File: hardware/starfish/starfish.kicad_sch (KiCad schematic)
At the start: 3 parts

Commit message: First pass at schematic for starfish
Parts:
- added H104: GND, MountingHole:MountingHole_3mm_Pad, symbol Mechanical:MountingHole_Pad
- renumbered H1 to H101, H2 to H102, H3 to H103
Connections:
- net GND: now also H104.1
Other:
- sheet Left Motor renamed X Motor
- sheet Right Motor renamed Y2 Motor
- sheet Z Motor renamed Y1 Motor
- added sheet Buffer (buffer.kicad_sch)
- added sheet I2C Multiplexer (i2c_mux.kicad_sch)
- added sheet Pump A (pumps.kicad_sch)
- added sheet Pump B (pumps.kicad_sch)
- added sheet RS485 (rs485.kicad_sch)
- added sheet Vacuum sensor A (vacuum-sensors.kicad_sch)
- added sheet Vacuum sensor B (vacuum-sensors.kicad_sch)
- added sheet Valve A (solenoids.kicad_sch)
- added sheet Valve B (solenoids.kicad_sch)
- sheet Connections ports: added QWIIC1_SCK, QWIIC1_SDA, QWIIC2_SCK, QWIIC2_SDA; removed BLTOUCH_CONTROL, BLTOUCH_OUT, QWIIC_SCL, QWIIC_SDA
- sheet Microcontroller ports: added I2C_SCL, I2C_SDA, PUMP_A, PUMP_B, RS485_OUT_EN, RS485_RX, RS485_TX, RS485_~{IN_EN}, VALVE_A, VALVE_B; removed BLTOUCH_CONTROL, BLTOUCH_STATUS, QWIIC_SCL, QWIIC_SDA
- title: Candela Head -> Starfish
- moved on the sheet: H101, H102, H103

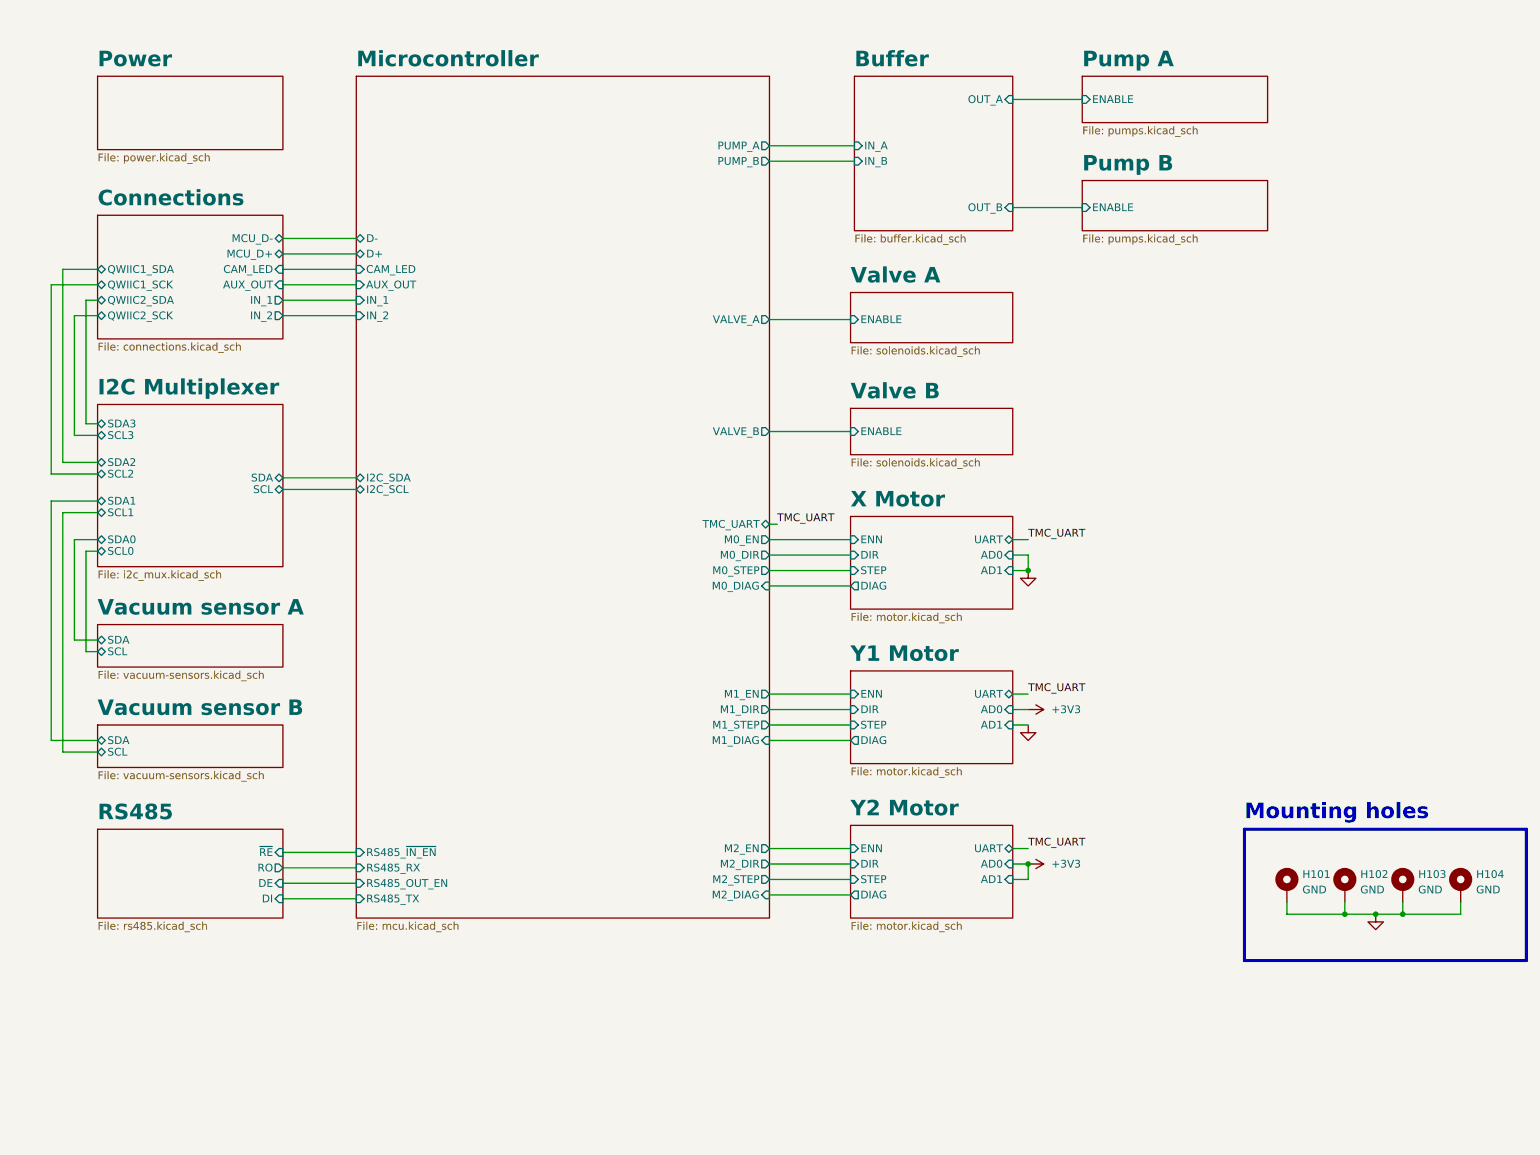
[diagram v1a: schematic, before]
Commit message: Mostly finished starfish schematic, ready for layout!
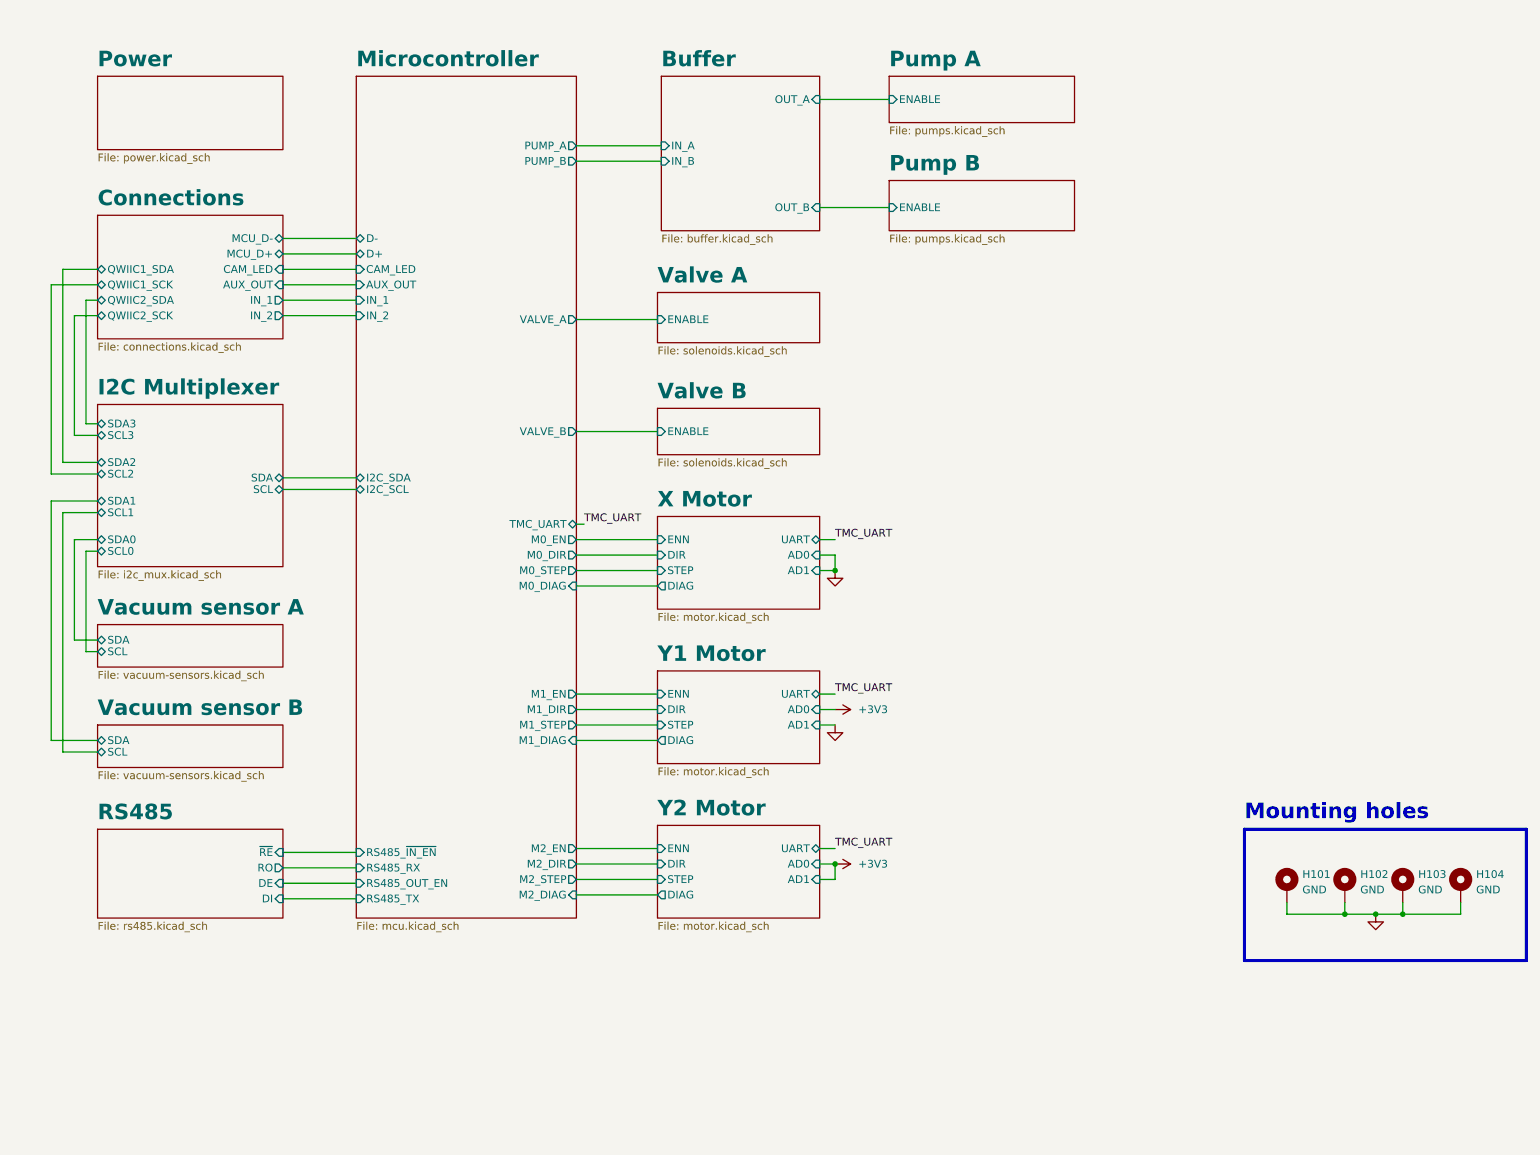
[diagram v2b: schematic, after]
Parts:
- H101, H102, H103, H104: mpn n/a -> (none)
